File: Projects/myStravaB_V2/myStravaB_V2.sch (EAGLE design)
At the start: 101 parts, among them IC1 TPS63051RMWT, Q2 BSS138BKW, T1 BC847, T2 BC847, U1 FXOS8700CQR1, U2 MCP73831, U4 NRF52840, Y2 32MHz, Y3 32.768kHz

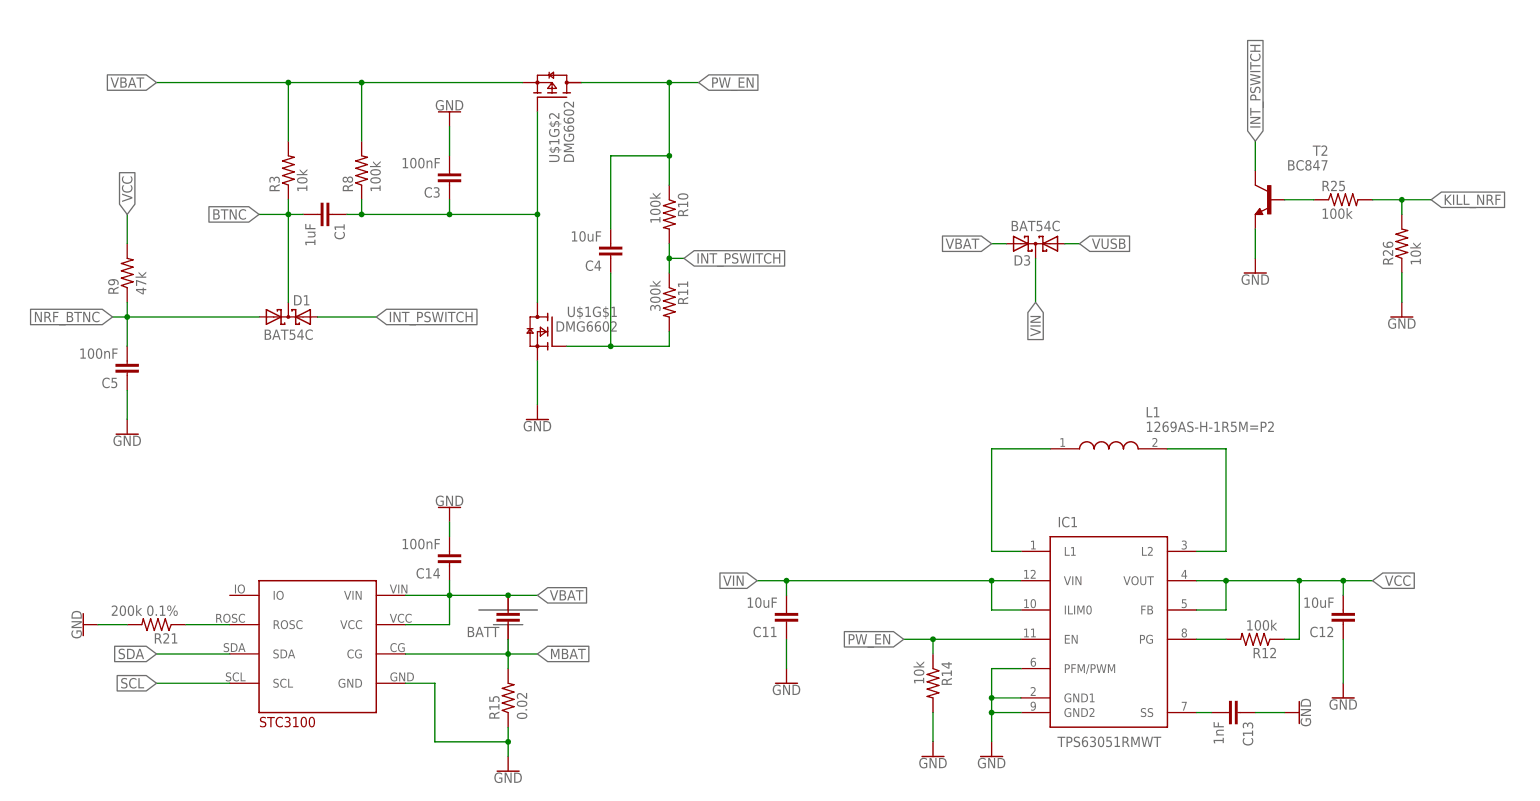
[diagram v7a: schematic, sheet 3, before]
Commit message: Added small capacitors More vias
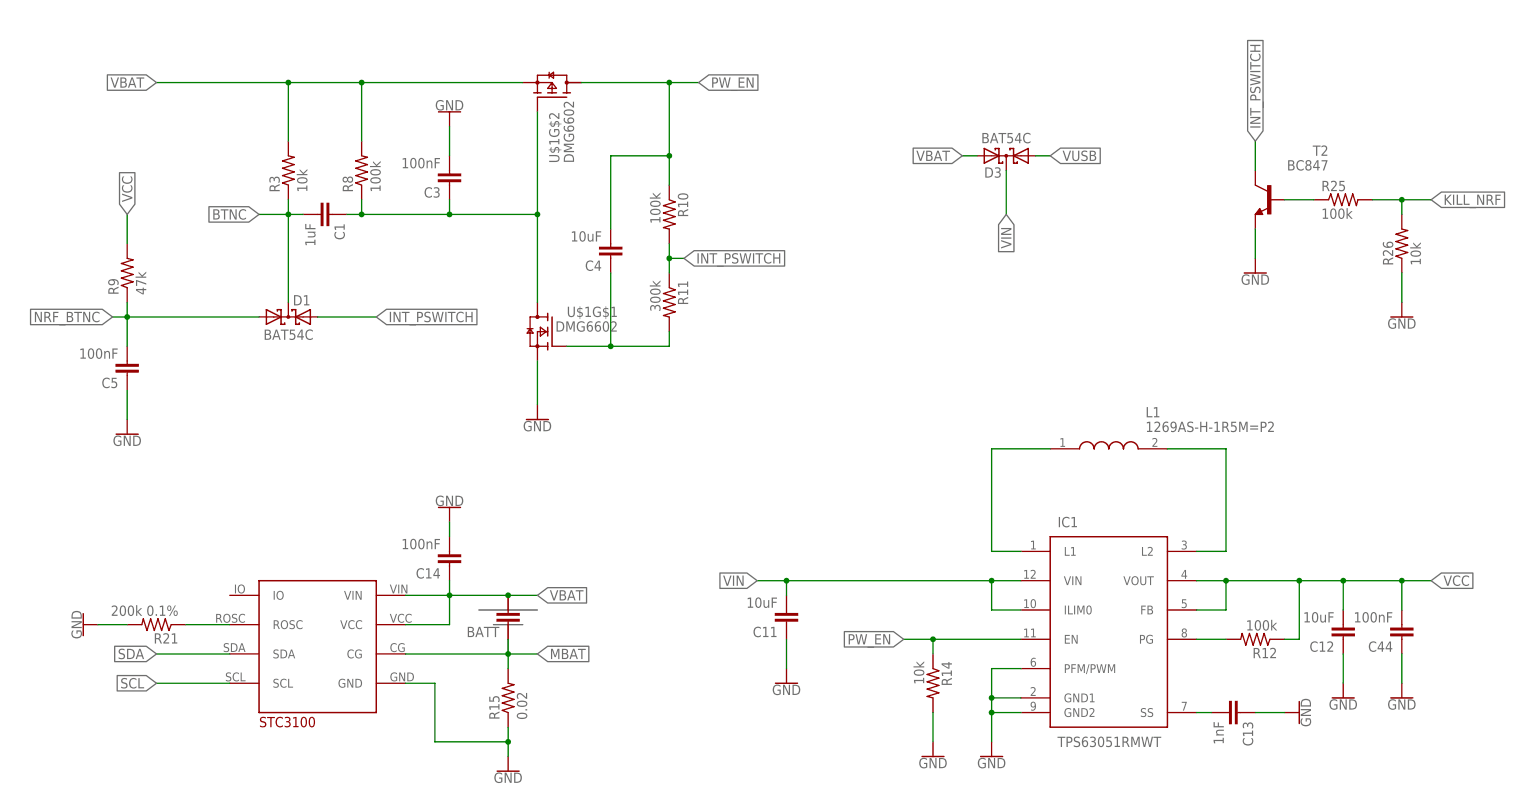
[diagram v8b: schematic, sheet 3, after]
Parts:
- added C19, C44: 100nF, rcl:C-EUC0603
- added C42: 1uF, rcl:C-EUC0603
- C12, C17: device rcl:C-EUC0805 -> rcl:C-EUC0603
- C15, C16: value 12pF -> 4.7uF
- C20: value 4.7uF -> 22uF; device rcl:C-EUC0805 -> rcl:C-EUC0603
- C32, C33: device rcl:C-EUC0402 -> rcl:C-EUC0603
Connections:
- net DECUSB: now also C42.1
- net GND: now also C19.2, C42.2, C44.1
- net VCC: now also C44.2
- net VUSB: now also C19.1
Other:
- moved on the sheet: C12, D3
